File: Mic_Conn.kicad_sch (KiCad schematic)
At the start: 23 parts, among them J1 JST_SUR_1x5_BM05B-SURS-TB-LF-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, J2 JST_SUR_1x5_BM05B-SURS-TB-LF-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, J8 JST_SUR_1x5_BM05B-SURS-TB-LF-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, U1 TPD4E05U06QDQARQ1, U6 TPD4E05U06QDQARQ1

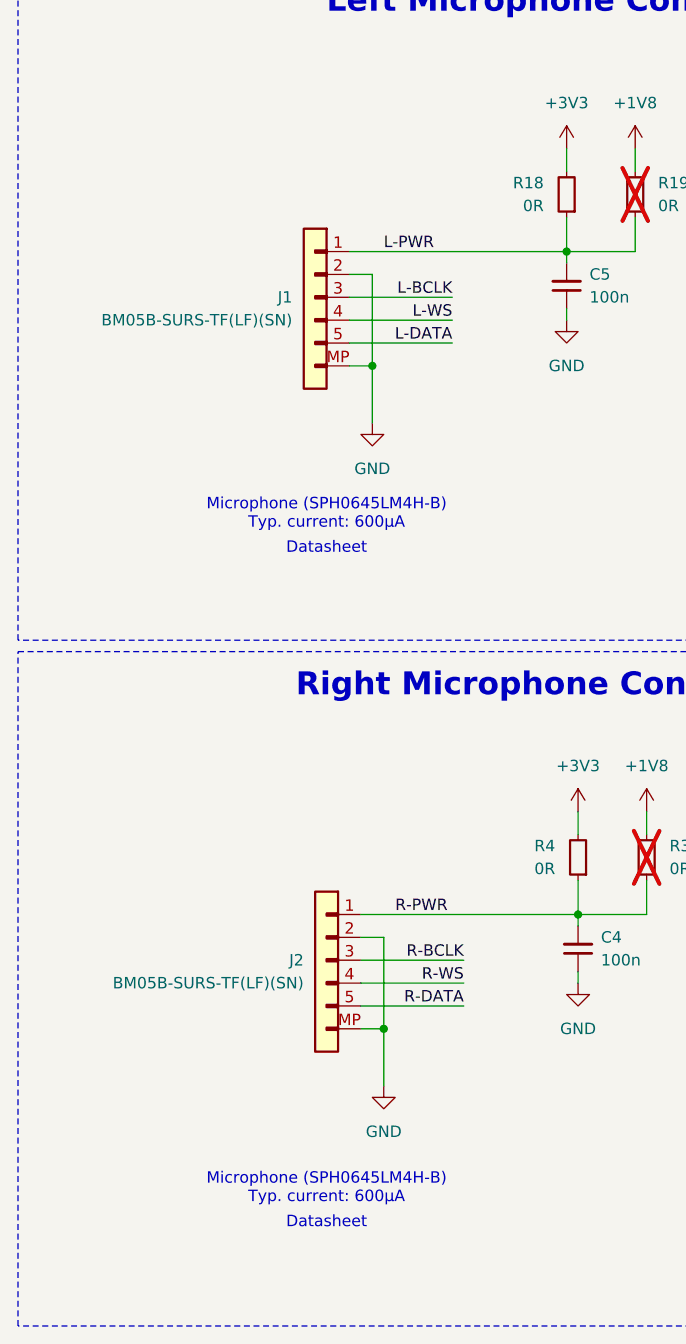
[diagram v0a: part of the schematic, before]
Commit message: [#71986] Replace microphone-board connectors with FFC/ZIF
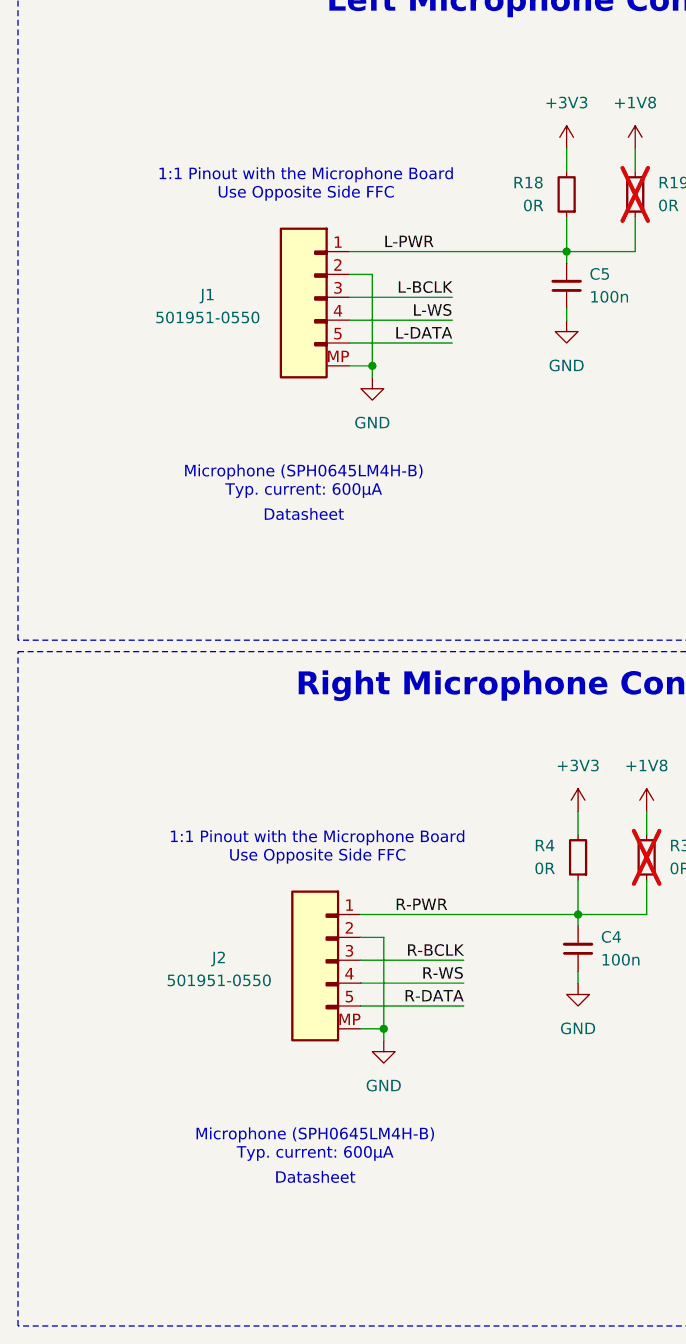
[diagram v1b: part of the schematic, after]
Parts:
- removed J1, J2: JST_SUR_1x5_BM05B-SURS-TB-LF-SN, antmicro-footprints:Conn_JST_SUR_1x5_BM05B-SURS-TF-LF-SN, symbol antmicroWire2BoardConnectors:JST_SUR_1x5_BM05B-SURS-TB-LF-SN
- added J1, J2: Conn_FFC_Molex_5019510550, antmicro-footprints:Conn_FFC_Molex_5019510550, symbol antmicroFCCConnectors:Conn_FFC_Molex_5019510550
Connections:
- net GND: now also J1.2, J1.MP, J2.2, J2.MP
- net L-BCLK: now also J1.3
- net L-DATA: now also J1.5
- net L-PWR: now also J1.1
- net L-WS: now also J1.4
- net R-BCLK: now also J2.3
- net R-DATA: now also J2.5
- net R-PWR: now also J2.1
- net R-WS: now also J2.4
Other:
- note added: "1:1 Pinout with the Microphone Board Use Opposite Side FFC"

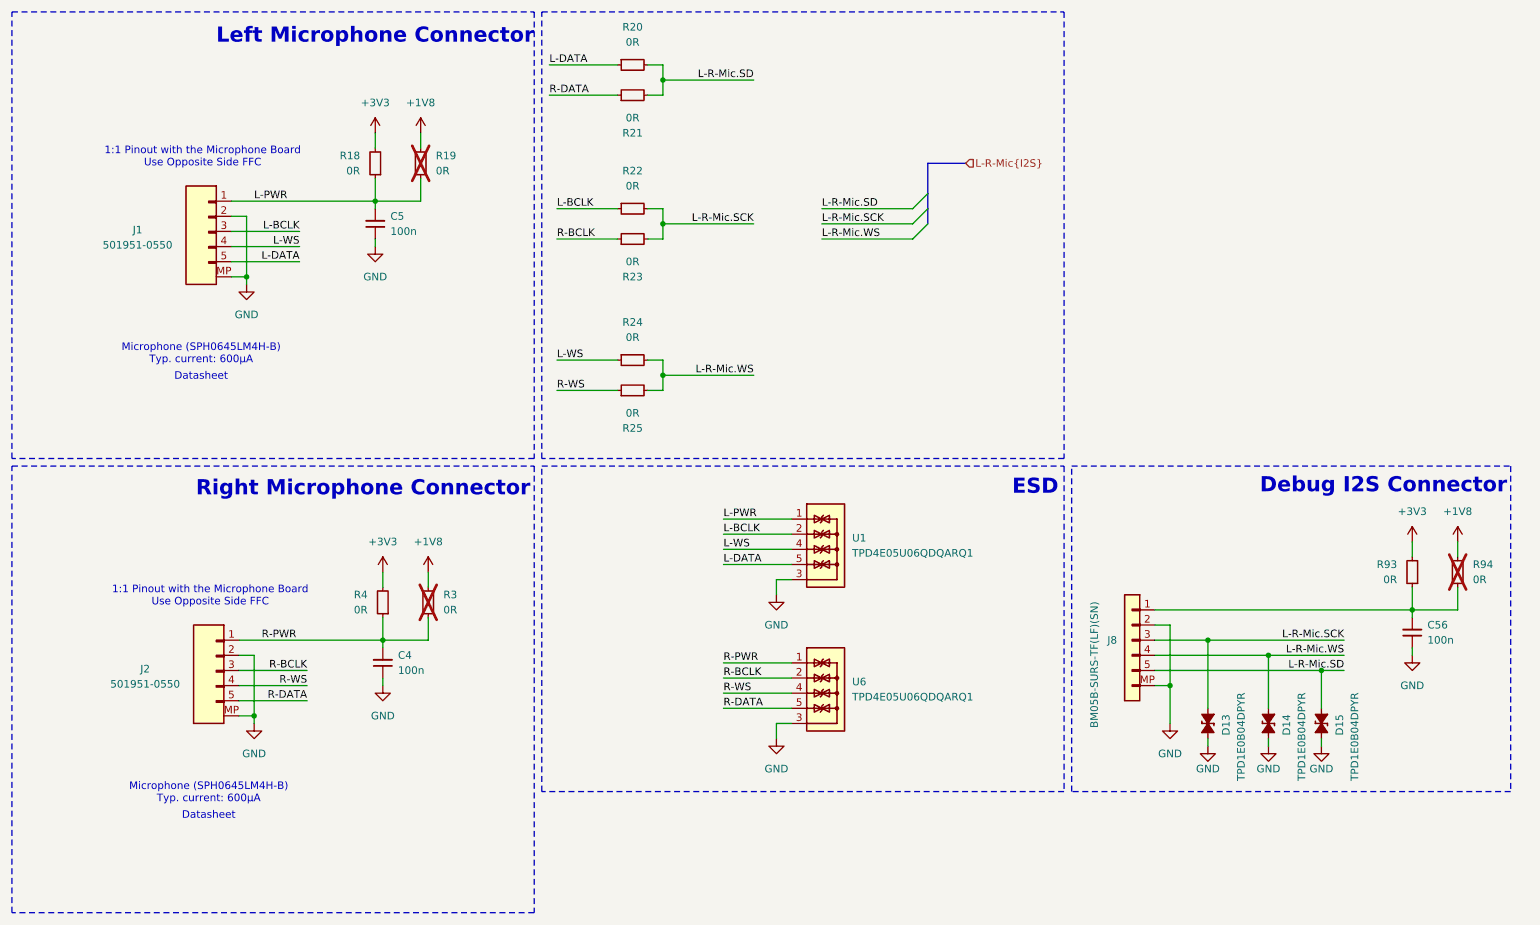
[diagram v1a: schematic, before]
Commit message: [#71986] Remove 1V8 circuits after changing the AMP
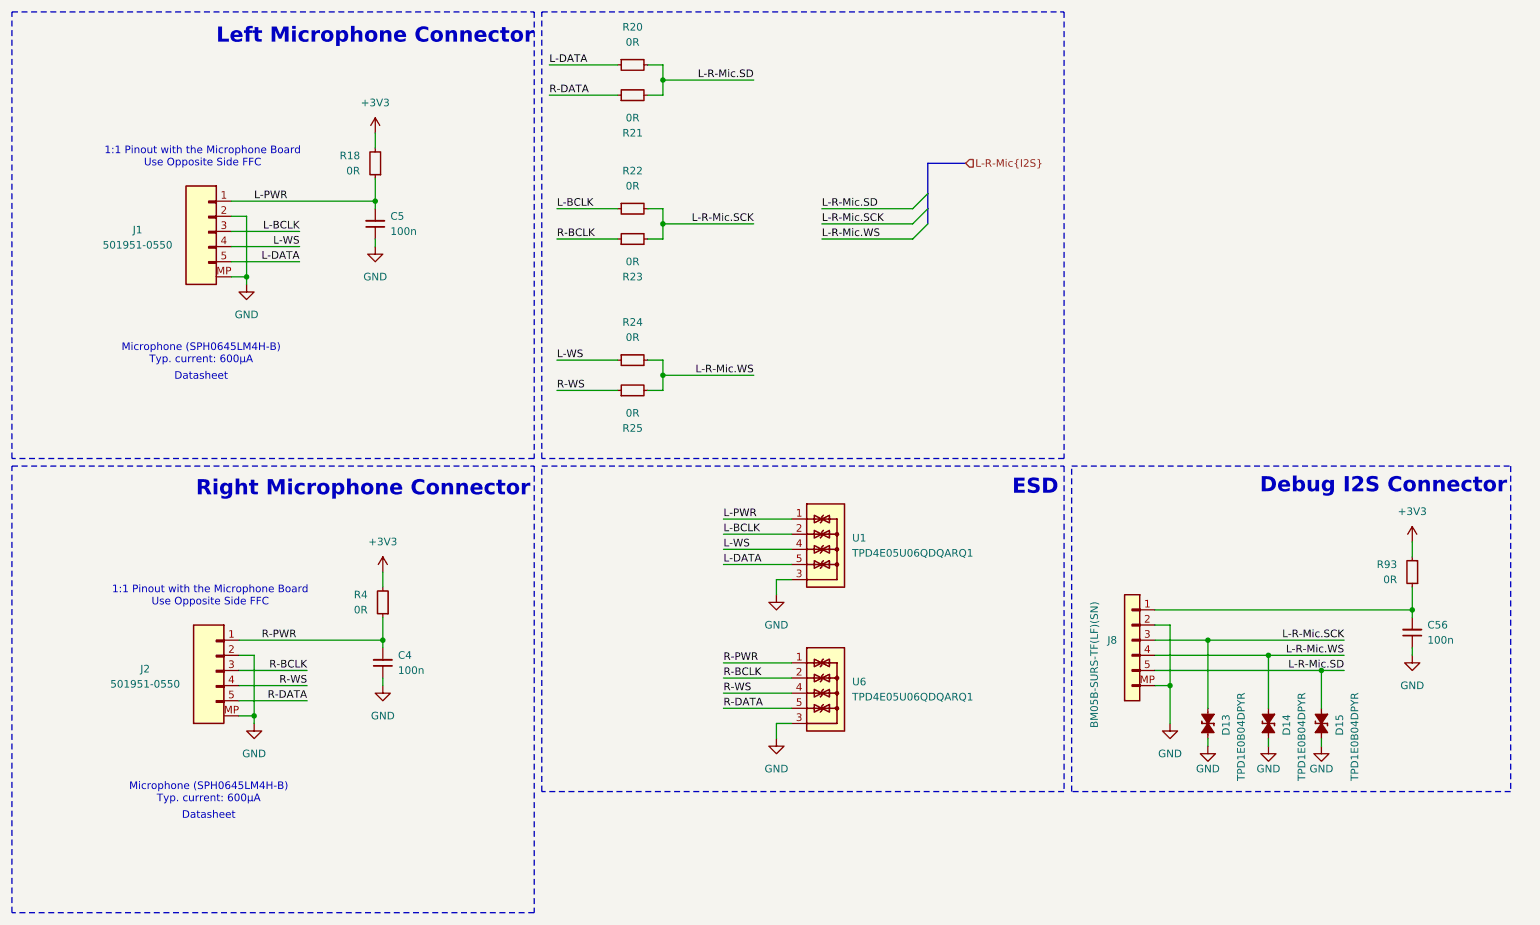
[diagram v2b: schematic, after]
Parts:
- removed R19, R3, R94: R_0R_0402, antmicro-footprints:R_0402_1005Metric, symbol antmicroResistors0402:R_0R_0402

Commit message: [#71249] Update project name
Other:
- title: Audio Latency Processing Board -> Audio controller board
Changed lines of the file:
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@@
 	(paper "A3")
 	(title_block
-		(title "Audio Latency Processing Board")
+		(title "Audio controller board")
 		(date "2025-01-20")
 		(rev "1.2.0")
@@
 		)
 		(instances
-			(project "audio-latency-processing-board"
+			(project "audio-controller-board"
 				(path "/7fb12ebf-f685-4412-b638-445b1bf344bc/a5973bba-065b-4f1e-8188-1e9f006e3cba"
 					(reference "R22")
@@
 		)
 		(instances
-			(project "audio-latency-processing-board"
+			(project "audio-controller-board"
 				(path "/7fb12ebf-f685-4412-b638-445b1bf344bc/a5973bba-065b-4f1e-8188-1e9f006e3cba"
 					(reference "D14")
@@
 		)
 		(instances
-			(project "audio-latency-processing-board"
+			(project "audio-controller-board"
 				(path "/7fb12ebf-f685-4412-b638-445b1bf344bc/a5973bba-065b-4f1e-8188-1e9f006e3cba"
 					(reference "#PWR05")
@@
 		)
 		(instances
-			(project "audio-latency-processing-board"
+			(project "audio-controller-board"
 				(path "/7fb12ebf-f685-4412-b638-445b1bf344bc/a5973bba-065b-4f1e-8188-1e9f006e3cba"
 					(reference "R18")
@@
 		)
 		(instances
-			(project "audio-latency-processing-board"
+			(project "audio-controller-board"
 				(path "/7fb12ebf-f685-4412-b638-445b1bf344bc/a5973bba-065b-4f1e-8188-1e9f006e3cba"
 					(reference "#PWR027")
@@
 		)
 		(instances
-			(project "audio-latency-processing-board"
+			(project "audio-controller-board"
 				(path "/7fb12ebf-f685-4412-b638-445b1bf344bc/a5973bba-065b-4f1e-8188-1e9f006e3cba"
 					(reference "#PWR0148")
@@
 		)
 		(instances
-			(project "audio-latency-processing-board"
+			(project "audio-controller-board"
 				(path "/7fb12ebf-f685-4412-b638-445b1bf344bc/a5973bba-065b-4f1e-8188-1e9f006e3cba"
 					(reference "#PWR0146")
@@
 		)
 		(instances
-			(project "audio-latency-processing-board"
+			(project "audio-controller-board"
 				(path "/7fb12ebf-f685-4412-b638-445b1bf344bc/a5973bba-065b-4f1e-8188-1e9f006e3cba"
 					(reference "C4")
@@
 		)
 		(instances
-			(project "audio-latency-processing-board"
+			(project "audio-controller-board"
 				(path "/7fb12ebf-f685-4412-b638-445b1bf344bc/a5973bba-065b-4f1e-8188-1e9f006e3cba"
 					(reference "D15")
@@
 		)
 		(instances
-			(project "audio-latency-processing-board"
+			(project "audio-controller-board"
 				(path "/7fb12ebf-f685-4412-b638-445b1bf344bc/a5973bba-065b-4f1e-8188-1e9f006e3cba"
 					(reference "#PWR03")
@@
 		)
 		(instances
-			(project "audio-latency-processing-board"
+			(project "audio-controller-board"
 				(path "/7fb12ebf-f685-4412-b638-445b1bf344bc/a5973bba-065b-4f1e-8188-1e9f006e3cba"
 					(reference "R21")
@@
 		)
 		(instances
-			(project "audio-latency-processing-board"
+			(project "audio-controller-board"
 				(path "/7fb12ebf-f685-4412-b638-445b1bf344bc/a5973bba-065b-4f1e-8188-1e9f006e3cba"
 					(reference "#PWR0147")
@@
 		)
 		(instances
-			(project "audio-latency-processing-board"
+			(project "audio-controller-board"
 				(path "/7fb12ebf-f685-4412-b638-445b1bf344bc/a5973bba-065b-4f1e-8188-1e9f006e3cba"
 					(reference "#PWR023")
@@
 		)
 		(instances
-			(project "audio-latency-processing-board"
+			(project "audio-controller-board"
 				(path "/7fb12ebf-f685-4412-b638-445b1bf344bc/a5973bba-065b-4f1e-8188-1e9f006e3cba"
 					(reference "C5")
@@
 		)
 		(instances
-			(project "audio-latency-processing-board"
+			(project "audio-controller-board"
 				(path "/7fb12ebf-f685-4412-b638-445b1bf344bc/a5973bba-065b-4f1e-8188-1e9f006e3cba"
 					(reference "R4")
@@
 		)
 		(instances
-			(project "audio-latency-processing-board"
+			(project "audio-controller-board"
 				(path "/7fb12ebf-f685-4412-b638-445b1bf344bc/a5973bba-065b-4f1e-8188-1e9f006e3cba"
 					(reference "C56")
@@
 		)
 		(instances
-			(project "audio-latency-processing-board"
+			(project "audio-controller-board"
 				(path "/7fb12ebf-f685-4412-b638-445b1bf344bc/a5973bba-065b-4f1e-8188-1e9f006e3cba"
 					(reference "J2")
@@
 		)
 		(instances
-			(project "audio-latency-processing-board"
+			(project "audio-controller-board"
 				(path "/7fb12ebf-f685-4412-b638-445b1bf344bc/a5973bba-065b-4f1e-8188-1e9f006e3cba"
 					(reference "J8")
@@
 		)
 		(instances
-			(project "audio-latency-processing-board"
+			(project "audio-controller-board"
 				(path "/7fb12ebf-f685-4412-b638-445b1bf344bc/a5973bba-065b-4f1e-8188-1e9f006e3cba"
 					(reference "R93")
@@
 		)
 		(instances
-			(project "audio-latency-processing-board"
+			(project "audio-controller-board"
 				(path "/7fb12ebf-f685-4412-b638-445b1bf344bc/a5973bba-065b-4f1e-8188-1e9f006e3cba"
 					(reference "U6")
@@
 		)
 		(instances
-			(project "audio-latency-processing-board"
+			(project "audio-controller-board"
 				(path "/7fb12ebf-f685-4412-b638-445b1bf344bc/a5973bba-065b-4f1e-8188-1e9f006e3cba"
 					(reference "R25")
@@
 		)
 		(instances
-			(project "audio-latency-processing-board"
+			(project "audio-controller-board"
 				(path "/7fb12ebf-f685-4412-b638-445b1bf344bc/a5973bba-065b-4f1e-8188-1e9f006e3cba"
 					(reference "#PWR0143")
@@
 		)
 		(instances
-			(project "audio-latency-processing-board"
+			(project "audio-controller-board"
 				(path "/7fb12ebf-f685-4412-b638-445b1bf344bc/a5973bba-065b-4f1e-8188-1e9f006e3cba"
 					(reference "#PWR024")
@@
 		)
 		(instances
-			(project "audio-latency-processing-board"
+			(project "audio-controller-board"
 				(path "/7fb12ebf-f685-4412-b638-445b1bf344bc/a5973bba-065b-4f1e-8188-1e9f006e3cba"
 					(reference "R24")
@@
 		)
 		(instances
-			(project "audio-latency-processing-board"
+			(project "audio-controller-board"
 				(path "/7fb12ebf-f685-4412-b638-445b1bf344bc/a5973bba-065b-4f1e-8188-1e9f006e3cba"
 					(reference "#PWR025")
@@
 		)
 		(instances
-			(project "audio-latency-processing-board"
+			(project "audio-controller-board"
 				(path "/7fb12ebf-f685-4412-b638-445b1bf344bc/a5973bba-065b-4f1e-8188-1e9f006e3cba"
 					(reference "#PWR0145")
@@
 		)
 		(instances
-			(project "audio-latency-processing-board"
+			(project "audio-controller-board"
 				(path "/7fb12ebf-f685-4412-b638-445b1bf344bc/a5973bba-065b-4f1e-8188-1e9f006e3cba"
 					(reference "R23")
@@
 		)
 		(instances
-			(project "audio-latency-processing-board"
+			(project "audio-controller-board"
 				(path "/7fb12ebf-f685-4412-b638-445b1bf344bc/a5973bba-065b-4f1e-8188-1e9f006e3cba"
 					(reference "D13")
@@
 		)
 		(instances
-			(project "audio-latency-processing-board"
+			(project "audio-controller-board"
 				(path "/7fb12ebf-f685-4412-b638-445b1bf344bc/a5973bba-065b-4f1e-8188-1e9f006e3cba"
 					(reference "R20")
@@
 		)
 		(instances
-			(project "audio-latency-processing-board"
+			(project "audio-controller-board"
 				(path "/7fb12ebf-f685-4412-b638-445b1bf344bc/a5973bba-065b-4f1e-8188-1e9f006e3cba"
 					(reference "#PWR0144")
@@
 		)
 		(instances
-			(project "audio-latency-processing-board"
+			(project "audio-controller-board"
 				(path "/7fb12ebf-f685-4412-b638-445b1bf344bc/a5973bba-065b-4f1e-8188-1e9f006e3cba"
 					(reference "#PWR026")

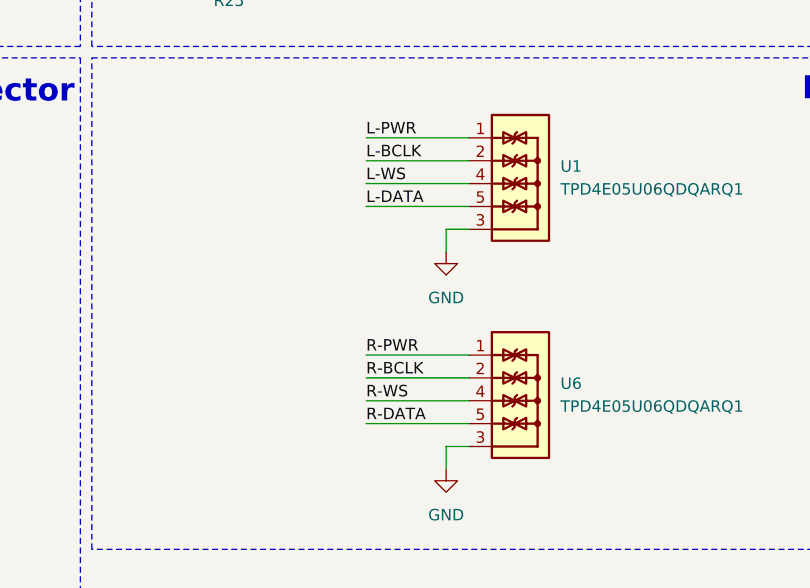
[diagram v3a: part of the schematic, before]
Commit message: [#71230] Replace speaker I2S ESD protection. Route speaker I2S lines
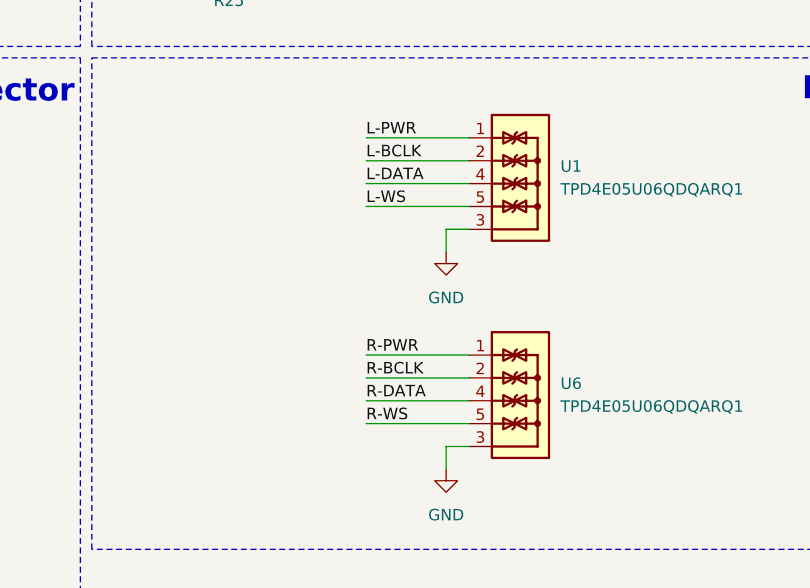
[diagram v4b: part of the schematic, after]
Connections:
- net L-DATA: now also U1.4, U1.7; no longer U1.5, U1.6
- net L-WS: now also U1.5, U1.6; no longer U1.4, U1.7
- net R-DATA: now also U6.4, U6.7; no longer U6.5, U6.6
- net R-WS: now also U6.5, U6.6; no longer U6.4, U6.7

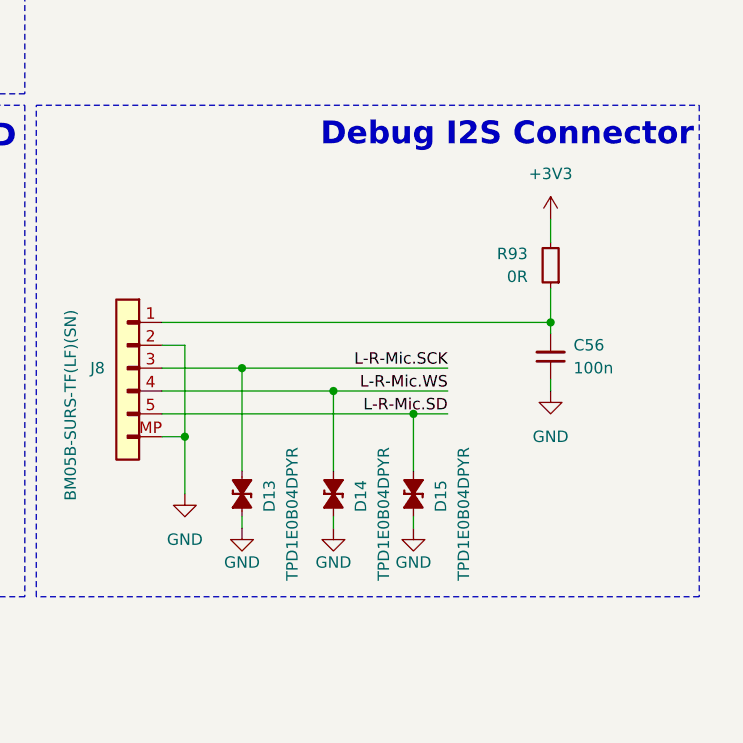
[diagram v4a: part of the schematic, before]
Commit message: [#71230] Route MCU1 I2S
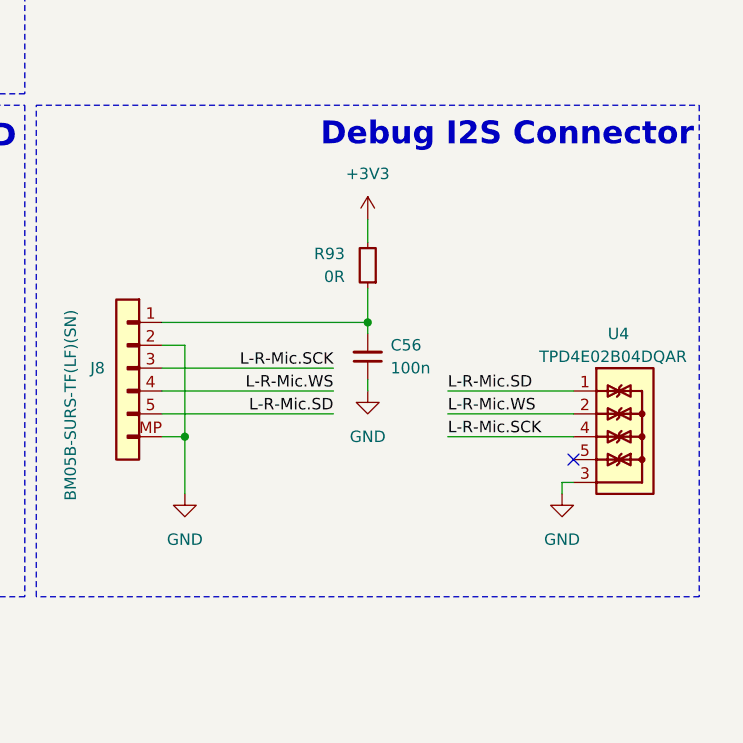
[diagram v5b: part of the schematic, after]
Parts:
- removed D13, D14, D15: TPD1E0B04_XDFN-2, antmicro-footprints:XDFN-2_1x0.60mm, symbol antmicroTVSDiodes:TPD1E0B04_XDFN-2
- added U4: TPD4E02B04DQA, antmicro-footprints:USON-10_2.5x1mm_P0.5mm, symbol antmicroTVSDiodes:TPD4E02B04DQA
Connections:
- net GND: now also U4.3, U4.8
- net L-R-Mic.SCK: now also U4.4, U4.7
- net L-R-Mic.SD: now also U4.1, U4.10
- net L-R-Mic.WS: now also U4.2, U4.9
- new net: U4.5, U4.6
- no-connect marks 0 -> 1
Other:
- moved on the sheet: C56, R93
